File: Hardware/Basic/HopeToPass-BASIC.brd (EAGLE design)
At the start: 38 x 38 mm, 48 parts, among them J2 FTDI_DEVICESMD, SW3 SWITCH.MOM, SW4 SWITCH.MOM, U1 NRF52832_MODULE_MDBT42, U2 PCF8523

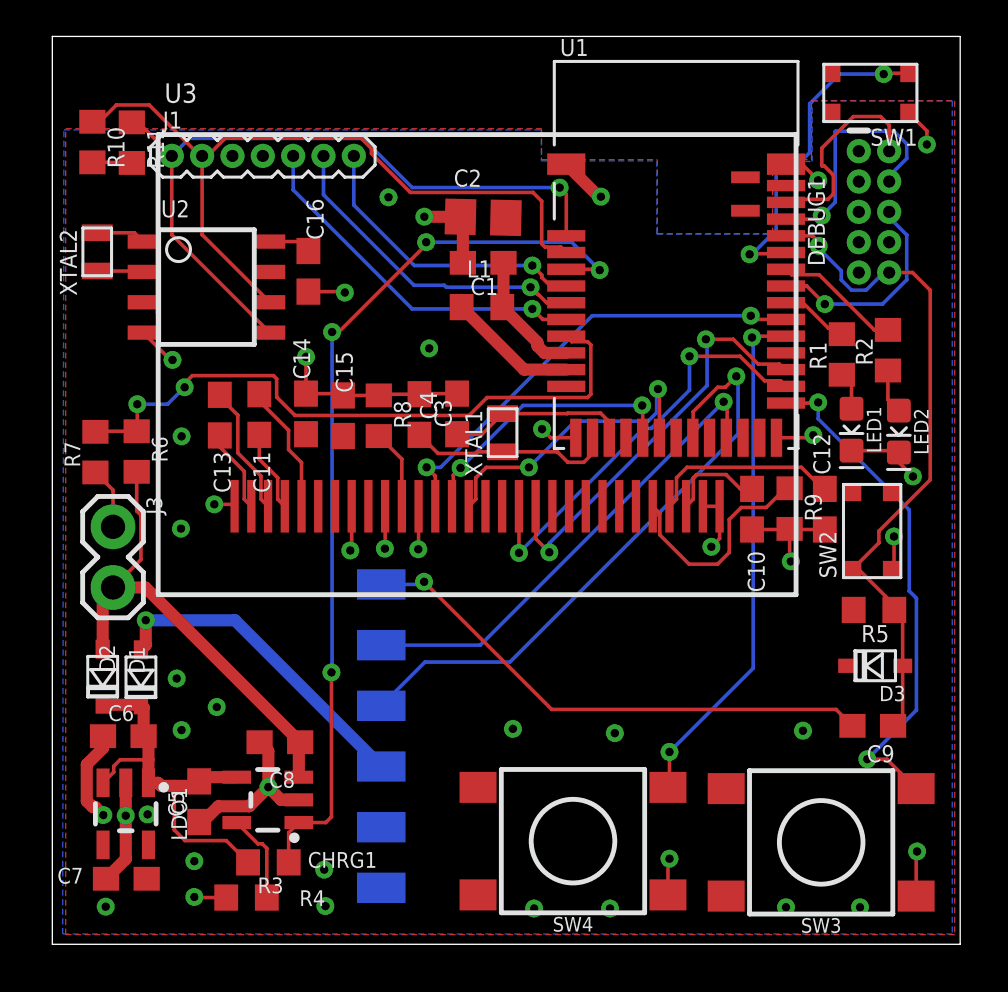
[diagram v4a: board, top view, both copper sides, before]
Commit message: added more ground vias and generated gerbers
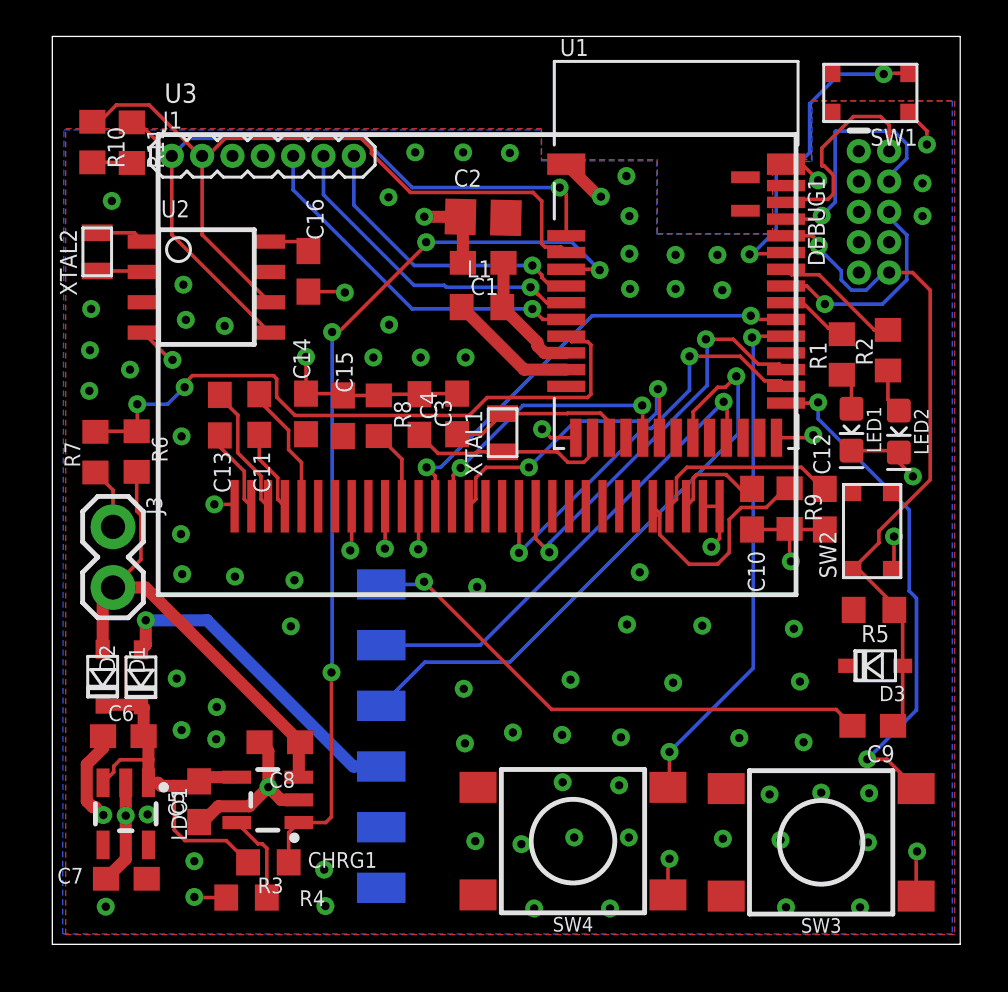
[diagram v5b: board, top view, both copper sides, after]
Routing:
- net GND: vias 42 -> 93
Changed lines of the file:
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@@
 <wire x1="31.7454" y1="21.2044" x2="31.8516" y2="21.3106" width="0.1524" layer="1"/>
 <via x="31.8516" y="21.3106" extent="1-16" drill="0.35"/>
-<via x="31.4198" y="8.9408" extent="1-16" drill="0.35"/>
+<via x="31.4452" y="8.4582" extent="1-16" drill="0.35"/>
 <via x="33.8074" y="1.5494" extent="1-16" drill="0.35"/>
 <via x="30.7086" y="1.5494" extent="1-16" drill="0.35"/>
-<via x="23.5458" y="8.8392" extent="1-16" drill="0.35"/>
+<via x="23.7998" y="8.6614" extent="1-16" drill="0.35"/>
 <via x="23.3426" y="1.4986" extent="1-16" drill="0.35"/>
 <via x="20.1676" y="1.4986" extent="1-16" drill="0.35"/>
-<via x="19.2786" y="9.017" extent="1-16" drill="0.35"/>
+<via x="19.2786" y="8.8646" extent="1-16" drill="0.35"/>
 <via x="11.43" y="1.6002" extent="1-16" drill="0.35"/>
 <via x="11.3792" y="3.1242" extent="1-16" drill="0.35"/>
@@
 <via x="6.8834" y="9.9314" extent="1-16" drill="0.35"/>
 <via x="5.207" y="11.1252" extent="1-16" drill="0.35"/>
-<via x="5.3848" y="17.399" extent="1-16" drill="0.35"/>
+<via x="5.3848" y="17.1704" extent="1-16" drill="0.35"/>
 <via x="5.4102" y="21.2598" extent="1-16" drill="0.35"/>
 <via x="5.0292" y="24.4602" extent="1-16" drill="0.35"/>
-<via x="15.7734" y="24.9428" extent="1-16" drill="0.35"/>
+<via x="15.4178" y="24.5618" extent="1-16" drill="0.35"/>
 <via x="12.2428" y="27.2796" extent="1-16" drill="0.35"/>
 <via x="14.0716" y="31.2674" extent="1-16" drill="0.35"/>
@@
 <vertex x="0.4318" y="0.4318"/>
 </polygon>
+<via x="17.7038" y="4.318" extent="1-16" drill="0.35"/>
+<via x="19.6342" y="4.191" extent="1-16" drill="0.35"/>
+<via x="21.844" y="4.4704" extent="1-16" drill="0.35"/>
+<via x="34.1376" y="4.2672" extent="1-16" drill="0.35"/>
+<via x="30.48" y="4.3688" extent="1-16" drill="0.35"/>
+<via x="1.5748" y="24.8666" extent="1-16" drill="0.35"/>
+<via x="1.6256" y="26.5938" extent="1-16" drill="0.35"/>
+<via x="17.2212" y="10.6934" extent="1-16" drill="0.35"/>
+<via x="24.0538" y="13.3858" extent="1-16" drill="0.35"/>
+<via x="27.2034" y="13.335" extent="1-16" drill="0.35"/>
+<via x="31.0388" y="13.208" extent="1-16" drill="0.35"/>
+<via x="6.858" y="8.5852" extent="1-16" drill="0.35"/>
+<via x="19.1516" y="33.1216" extent="1-16" drill="0.35"/>
+<via x="17.1958" y="33.147" extent="1-16" drill="0.35"/>
+<via x="15.1892" y="33.147" extent="1-16" drill="0.35"/>
+<via x="7.2136" y="25.8826" extent="1-16" drill="0.35"/>
+<via x="5.588" y="26.1366" extent="1-16" drill="0.35"/>
+<via x="5.4864" y="27.6098" extent="1-16" drill="0.35"/>
+<via x="14.097" y="25.9334" extent="1-16" drill="0.35"/>
+<via x="10.1346" y="15.24" extent="1-16" drill="0.35"/>
+<via x="5.4356" y="15.494" extent="1-16" drill="0.35"/>
+<via x="2.4892" y="31.115" extent="1-16" drill="0.35"/>
+<via x="24.1554" y="30.48" extent="1-16" drill="0.35"/>
+<via x="24.0284" y="32.1564" extent="1-16" drill="0.35"/>
+<via x="24.1808" y="27.432" extent="1-16" drill="0.35"/>
+<via x="26.0858" y="27.432" extent="1-16" drill="0.35"/>
+<via x="27.8384" y="28.8544" extent="1-16" drill="0.35"/>
+<via x="28.0416" y="27.3812" extent="1-16" drill="0.35"/>
+<via x="24.5872" y="15.5702" extent="1-16" drill="0.35"/>
+<via x="25.9842" y="10.9474" extent="1-16" drill="0.35"/>
+<via x="21.3614" y="6.7818" extent="1-16" drill="0.35"/>
+<via x="28.067" y="4.4196" extent="1-16" drill="0.35"/>
+<via x="13.4366" y="24.5618" extent="1-16" drill="0.35"/>
+<via x="1.5494" y="23.1648" extent="1-16" drill="0.35"/>
+<via x="3.2512" y="24.0538" extent="1-16" drill="0.35"/>
+<via x="24.1554" y="28.9052" extent="1-16" drill="0.35"/>
+<via x="26.0858" y="28.8544" extent="1-16" drill="0.35"/>
+<via x="31.2928" y="10.9982" extent="1-16" drill="0.35"/>
+<via x="21.6916" y="11.0744" extent="1-16" drill="0.35"/>
+<via x="17.272" y="8.4074" extent="1-16" drill="0.35"/>
+<via x="21.336" y="8.763" extent="1-16" drill="0.35"/>
+<via x="23.7236" y="6.6548" extent="1-16" drill="0.35"/>
+<via x="24.13" y="4.4704" extent="1-16" drill="0.35"/>
+<via x="28.7528" y="8.636" extent="1-16" drill="0.35"/>
+<via x="30.0228" y="6.2738" extent="1-16" drill="0.35"/>
+<via x="32.1818" y="6.35" extent="1-16" drill="0.35"/>
+<via x="34.1884" y="6.3246" extent="1-16" drill="0.35"/>
+<via x="7.6454" y="15.3924" extent="1-16" drill="0.35"/>
+<via x="9.9822" y="13.3096" extent="1-16" drill="0.35"/>
+<via x="17.2974" y="24.5618" extent="1-16" drill="0.35"/>
+<via x="17.78" y="14.9606" extent="1-16" drill="0.35"/>
 </signal>
 <signal name="N$4">
@@
 <contactref element="D2" pad="+"/>
 <contactref element="J2" pad="VCC"/>
-<wire x1="13.7668" y1="7.4422" x2="7.6454" y2="13.5636" width="0.508" layer="16"/>
-<wire x1="7.6454" y1="13.5636" x2="3.9116" y2="13.5636" width="0.508" layer="16"/>
+<wire x1="13.7668" y1="7.4422" x2="12.5984" y2="7.4422" width="0.508" layer="16"/>
+<wire x1="12.5984" y1="7.4422" x2="6.477" y2="13.5636" width="0.508" layer="16"/>
+<wire x1="6.477" y1="13.5636" x2="3.9116" y2="13.5636" width="0.508" layer="16"/>
 <via x="3.9116" y="13.5636" extent="1-16" drill="0.35"/>
 <wire x1="3.9116" y1="13.5636" x2="3.9116" y2="12.5292" width="0.508" layer="1"/>
@@
 <contactref element="U2" pad="3"/>
 </signal>
+<signal name="N$25">
+<via x="36.4236" y="31.8516" extent="1-16" drill="0.35"/>
+</signal>
+<signal name="N$26">
+<via x="36.4236" y="30.48" extent="1-16" drill="0.35"/>
+</signal>
 </signals>
